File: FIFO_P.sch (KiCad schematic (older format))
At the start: 51 parts, among them J1 Vin +, J2 Vin -, J3 Conn_Coaxial, SW1 Rotary_Encoder_61C, U1 SN74LVC2G157_MUX_TI, U10 AD7840, U2 IDT_ICS551, U3 LTC1740, U4 ARDUINO_DUE_FIFO_P_COMMANDS, U5 IDT_72V2105, U6 TXB0104, U7 TXB0104, U8 TXB0104, U9 TXB0104

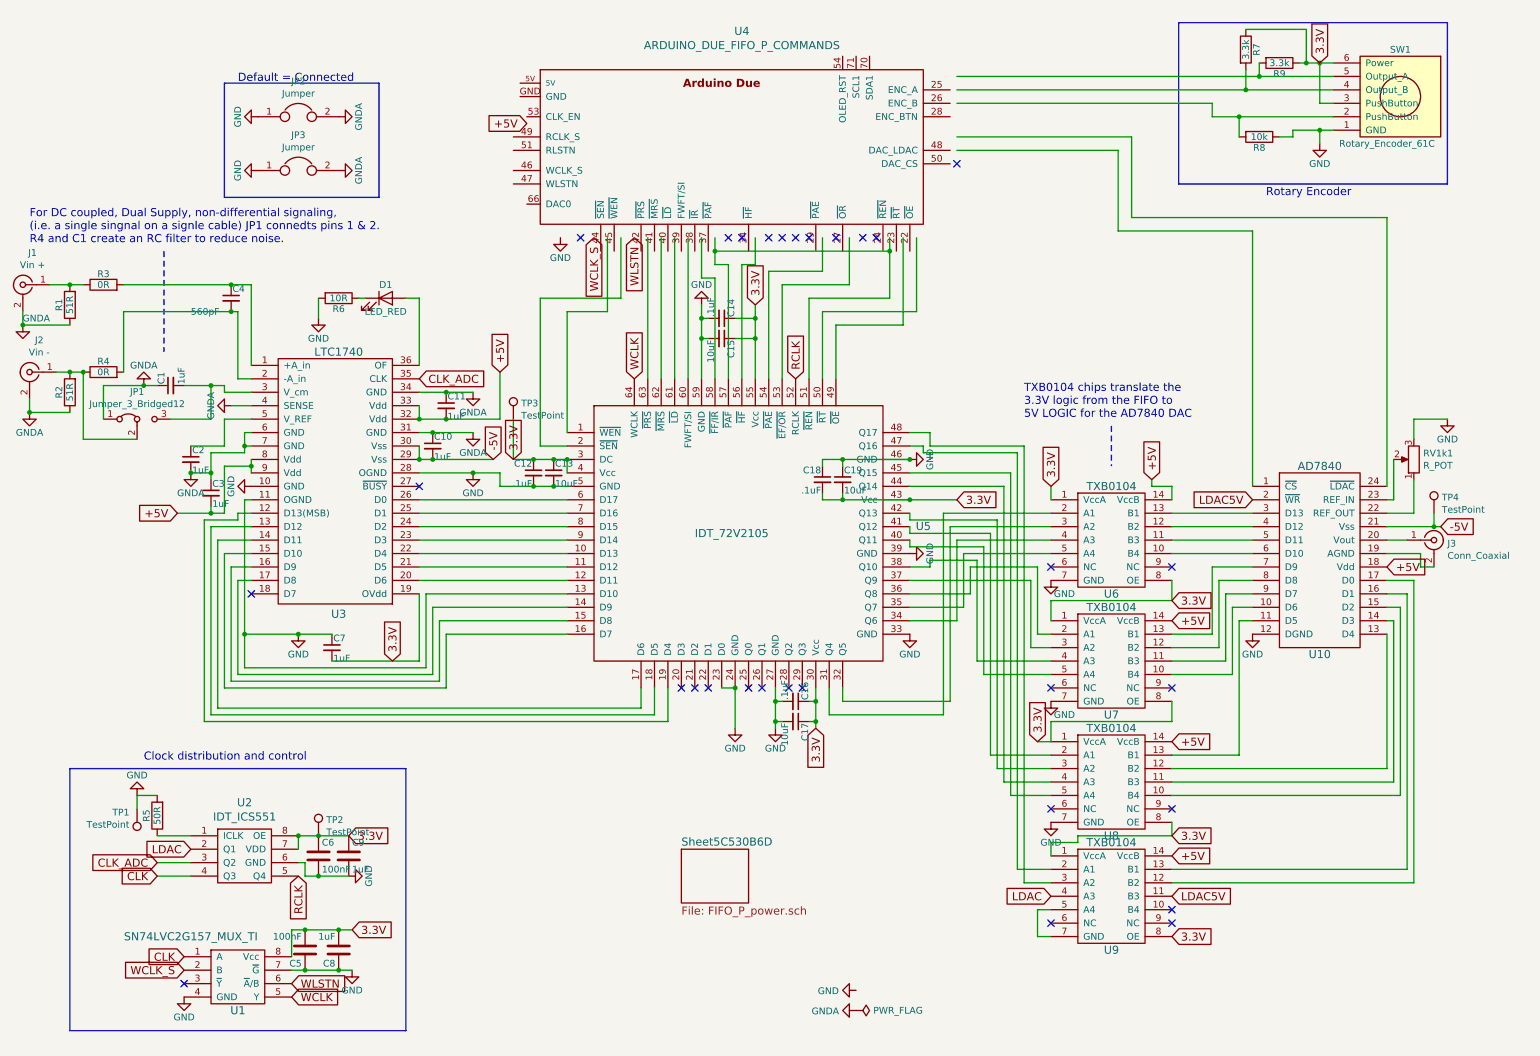
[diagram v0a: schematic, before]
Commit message: Fix arduino header, started laying out connectors
The pins used were changed, so the old code must be rewritten to use the new pins and port D instead of port A.
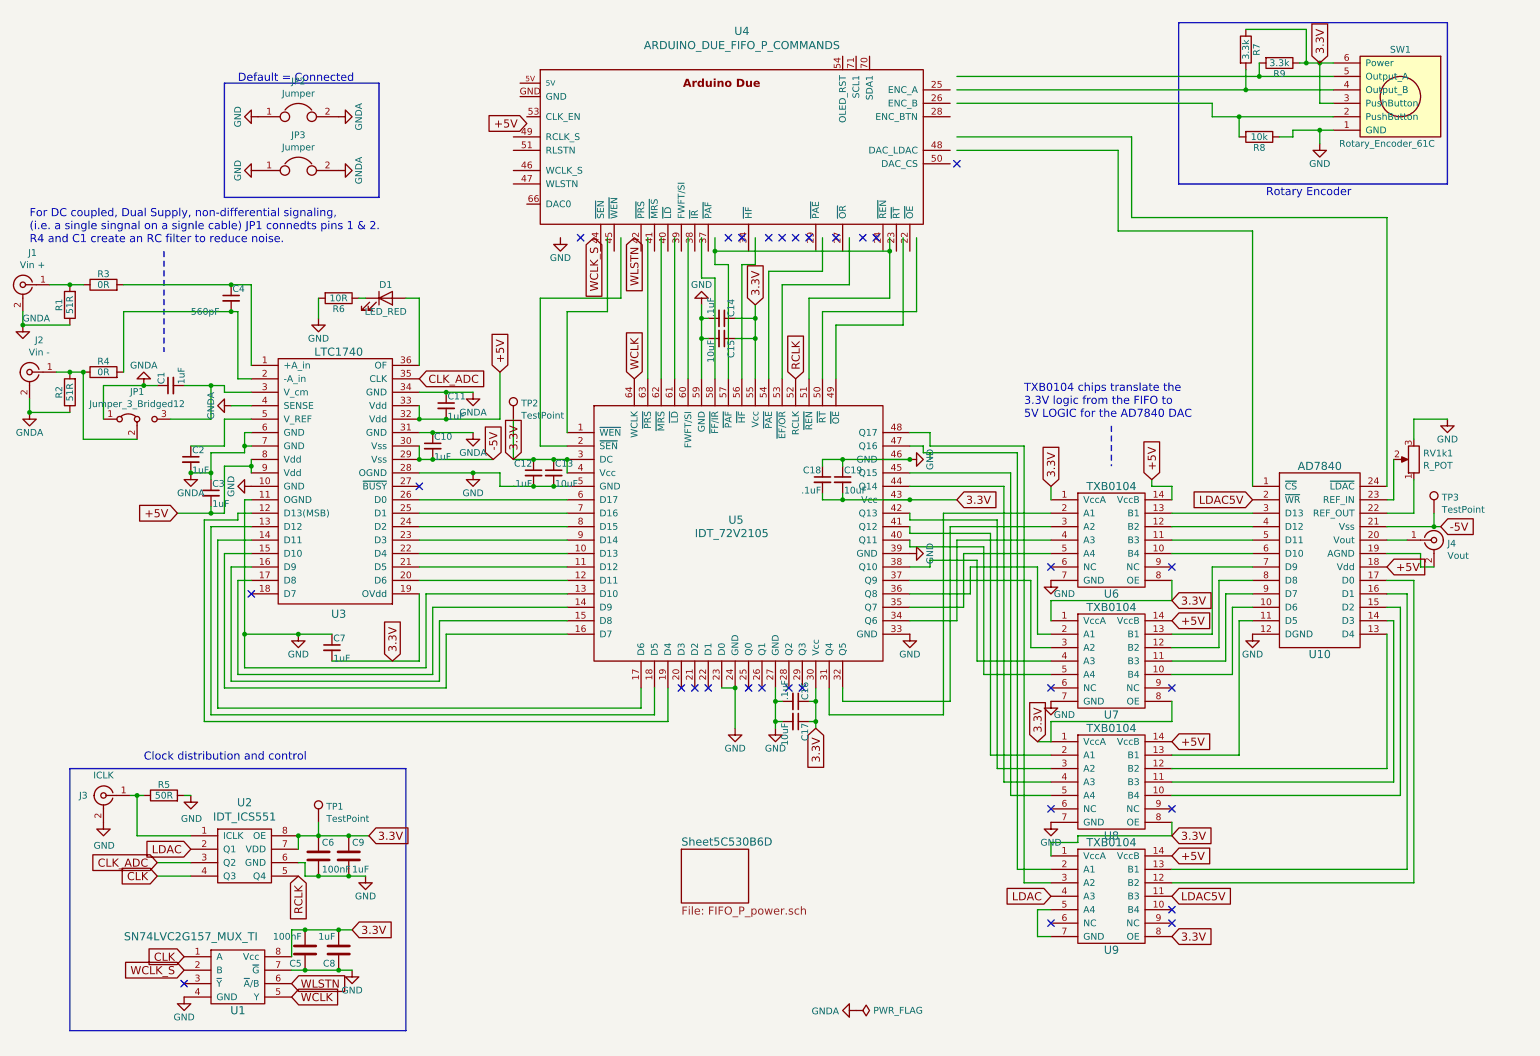
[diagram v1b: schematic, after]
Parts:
- removed TP1: TestPoint, FIFO_P:Test_Pin, symbol Connector:TestPoint
- added J3: ICLK, Connector_Coaxial:BNC_TEConnectivity_1478204_Vertical, symbol Connector:Conn_Coaxial
- J4: renamed from J3; value Conn_Coaxial -> Vout
- renumbered TP2 to TP1, TP3 to TP2, TP4 to TP3
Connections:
- wire segments 358 -> 363
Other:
- moved on the sheet: R5, TP1

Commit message: ADC to FIFO routing
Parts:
- U5: footprint Package_QFP:LQFP-160_24x24mm_P0.5mm -> Package_QFP:LQFP-64_14x14mm_P0.8mm
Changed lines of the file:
@@
 F 0 "U5" H 5650 4200 60  0000 L CNN
 F 1 "IDT_72V2105" H 5400 4100 60  0000 L CNN
-F 2 "Package_QFP:LQFP-160_24x24mm_P0.5mm" H 5700 4100 60  0001 C CNN
+F 2 "Package_QFP:LQFP-64_14x14mm_P0.8mm" H 5700 4100 60  0001 C CNN
 F 3 "" H 5700 4100 60  0000 C CNN
 	1    5700 4100

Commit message: Most routing done
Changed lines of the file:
@@
 	0    1    1    0
 $EndComp
+$Comp
+L power:GND #PWR0101
+U 1 1 5D0F24EC
+P 7950 7100
+F 0 "#PWR0101" H 7950 6850 50  0001 C CNN
+F 1 "GND" H 7955 6927 50  0000 C CNN
+F 2 "" H 7950 7100 50  0001 C CNN
+F 3 "" H 7950 7100 50  0001 C CNN
+	1    7950 7100
+	1    0    0    -1
+$EndComp
+Connection ~ 7950 7100
 $EndSCHEMATC

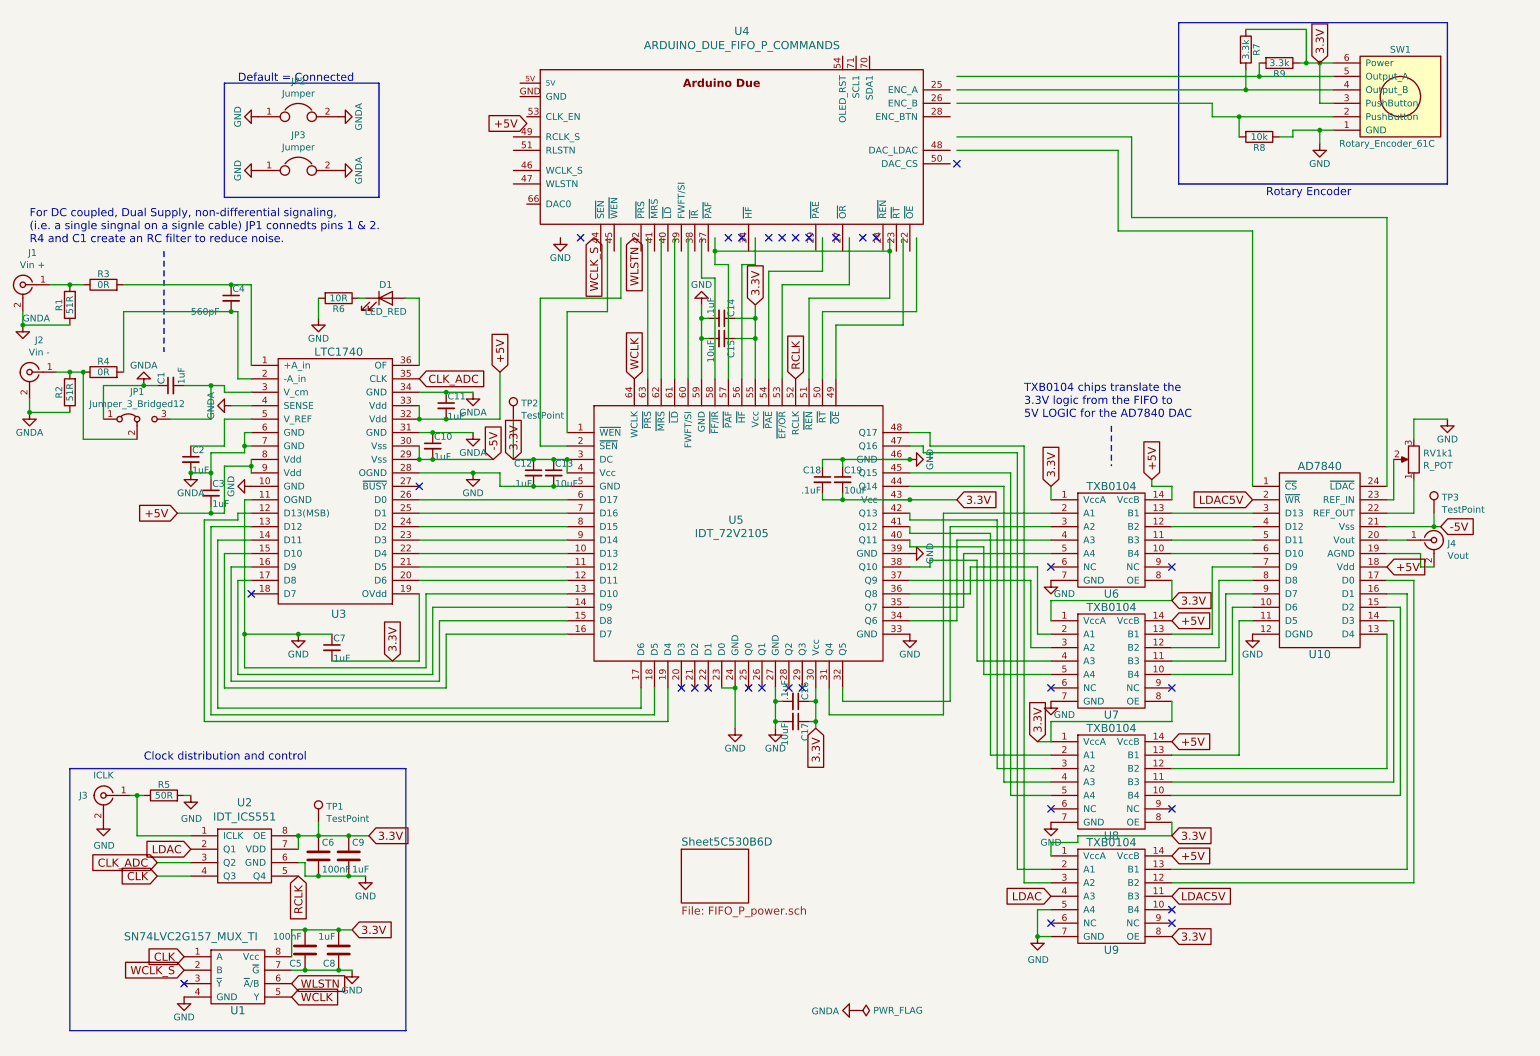
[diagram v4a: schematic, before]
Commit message: Partial jumpers
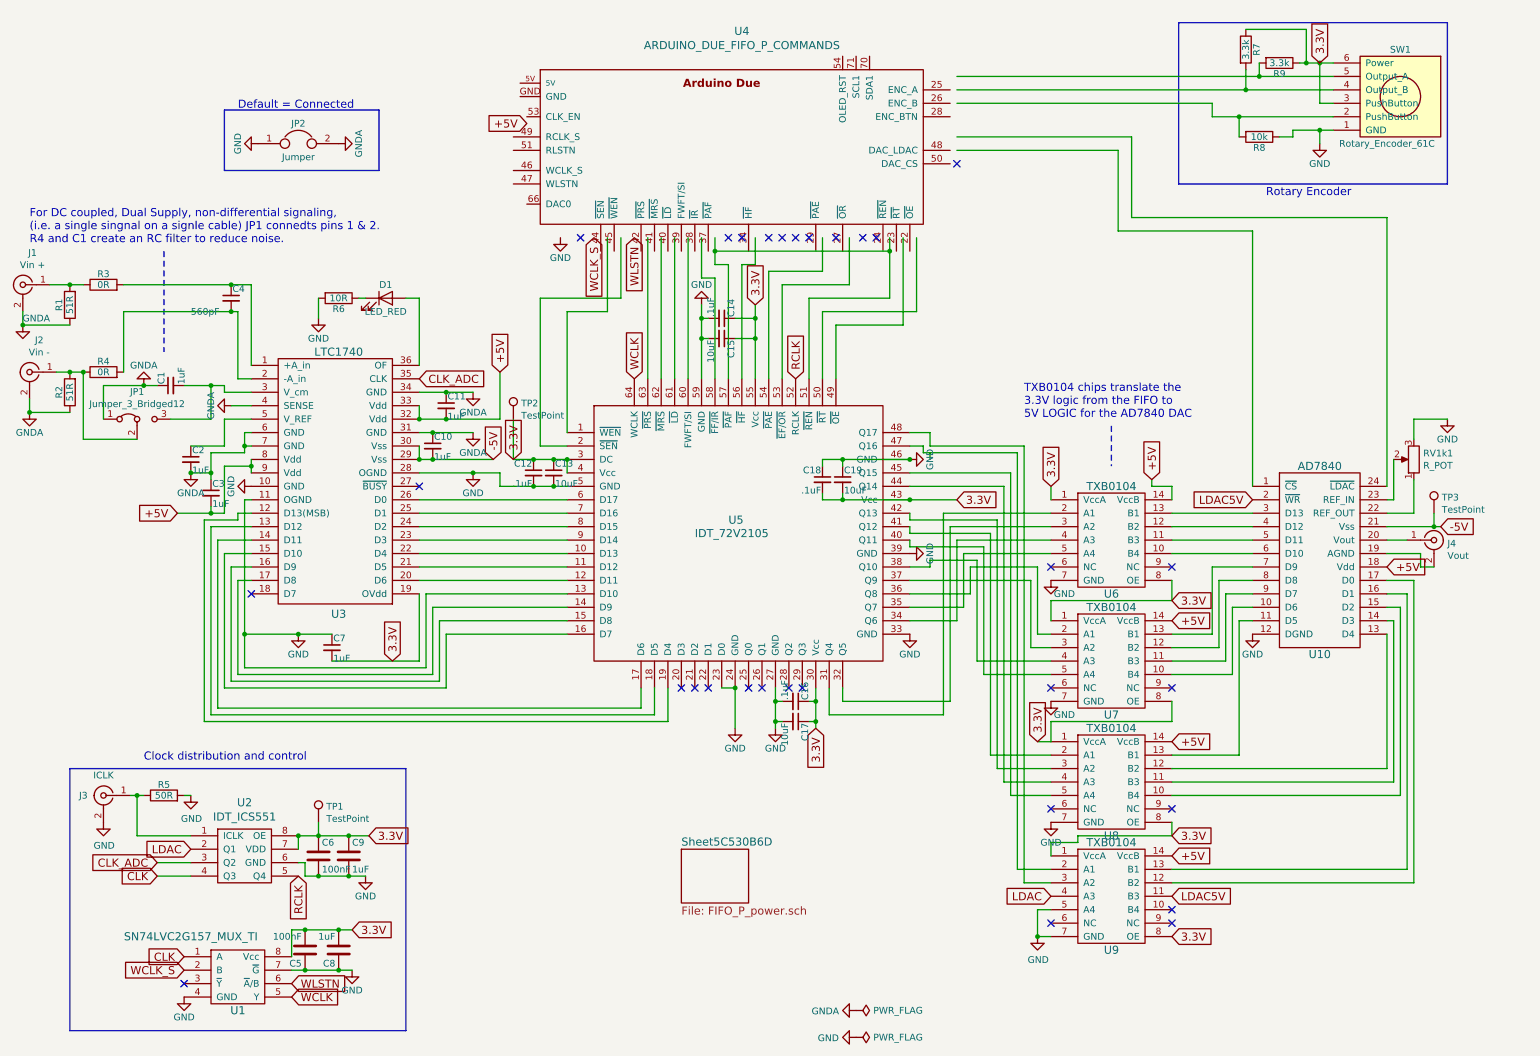
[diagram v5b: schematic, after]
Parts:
- removed JP3: Jumper, Connector_PinHeader_2.54mm:PinHeader_1x02_P2.54mm_Vertical, symbol Device:Jumper
- JP1: footprint Connector_PinHeader_2.54mm:PinHeader_1x02_P2.54mm_Vertical -> Jumper:SolderJumper-3_P1.3mm_Open_RoundedPad1.0x1.5mm
- R3, R4: footprint Resistor_THT:R_Axial_DIN0204_L3.6mm_D1.6mm_P7.62mm_Horizontal -> Resistor_THT:R_Axial_DIN0204_L3.6mm_D1.6mm_P5.08mm_Horizontal
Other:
- moved on the sheet: JP2
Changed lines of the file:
@@
 F 0 "R3" V 1080 2250 50  0000 C CNN
 F 1 "0R" V 1000 2250 50  0000 C CNN
-F 2 "Resistor_THT:R_Axial_DIN0204_L3.6mm_D1.6mm_P7.62mm_Horizontal" V 930 2250 50  0001 C CNN
+F 2 "Resistor_THT:R_Axial_DIN0204_L3.6mm_D1.6mm_P5.08mm_Horizontal" V 930 2250 50  0001 C CNN
 F 3 "" H 1000 2250 50  0000 C CNN
 	1    1000 2250
@@
 F 0 "R4" V 1080 2900 50  0000 C CNN
 F 1 "0R" V 1000 2900 50  0000 C CNN
-F 2 "Resistor_THT:R_Axial_DIN0204_L3.6mm_D1.6mm_P7.62mm_Horizontal" V 930 2900 50  0001 C CNN
+F 2 "Resistor_THT:R_Axial_DIN0204_L3.6mm_D1.6mm_P5.08mm_Horizontal" V 930 2900 50  0001 C CNN
 F 3 "" H 1000 2900 50  0000 C CNN
 	1    1000 2900
@@
 L power:GND #PWR010
 U 1 1 592DEA1F
-P 2150 1000
-F 0 "#PWR010" H 2150 750 50  0001 C CNN
-F 1 "GND" H 2150 850 50  0000 C CNN
-F 2 "" H 2150 1000 50  0000 C CNN
-F 3 "" H 2150 1000 50  0000 C CNN
-	1    2150 1000
+P 2150 1200
+F 0 "#PWR010" H 2150 950 50  0001 C CNN
+F 1 "GND" H 2150 1050 50  0000 C CNN
+F 2 "" H 2150 1200 50  0000 C CNN
+F 3 "" H 2150 1200 50  0000 C CNN
+	1    2150 1200
 	0    1    1    0
 $EndComp
@@
 L power:GNDA #PWR014
 U 1 1 592DEAA9
-P 2750 1000
-F 0 "#PWR014" H 2750 750 50  0001 C CNN
-F 1 "GNDA" H 2750 850 50  0000 C CNN
-F 2 "" H 2750 1000 50  0000 C CNN
-F 3 "" H 2750 1000 50  0000 C CNN
-	1    2750 1000
-	0    -1   -1   0
-$EndComp
-$Comp
-L power:GND #PWR011
-U 1 1 592DEB87
-P 2150 1400
-F 0 "#PWR011" H 2150 1150 50  0001 C CNN
-F 1 "GND" H 2150 1250 50  0000 C CNN
-F 2 "" H 2150 1400 50  0000 C CNN
-F 3 "" H 2150 1400 50  0000 C CNN
-	1    2150 1400
-	0    1    1    0
-$EndComp
-$Comp
-L power:GNDA #PWR015
-U 1 1 592DEB8D
-P 2750 1400
-F 0 "#PWR015" H 2750 1150 50  0001 C CNN
-F 1 "GNDA" H 2750 1250 50  0000 C CNN
-F 2 "" H 2750 1400 50  0000 C CNN
-F 3 "" H 2750 1400 50  0000 C CNN
-	1    2750 1400
+P 2750 1200
+F 0 "#PWR014" H 2750 950 50  0001 C CNN
+F 1 "GNDA" H 2750 1050 50  0000 C CNN
+F 2 "" H 2750 1200 50  0000 C CNN
+F 3 "" H 2750 1200 50  0000 C CNN
+	1    2750 1200
 	0    -1   -1   0
 $EndComp
@@
 	1    0    0    -1
 $EndComp
-Text Notes 2000 750  0    60   ~ 0
+Text Notes 2000 950  0    60   ~ 0
 Default = Connected
 Wire Bus Line
-	1900 750  3050 750
+	1900 950  3050 950
 Wire Bus Line
-	3050 750  3050 1600
+	3050 950  3050 1400
 Wire Bus Line
-	3050 1600 1900 1600
+	3050 1400 1900 1400
 Wire Bus Line
-	1900 1600 1900 750
+	1900 1400 1900 950
 Wire Bus Line
 	750  5850 750  7800
@@
 F 0 "JP1" H 1250 3454 50  0000 C CNN
 F 1 "Jumper_3_Bridged12" H 1250 3363 50  0000 C CNN
-F 2 "Connector_PinHeader_2.54mm:PinHeader_1x02_P2.54mm_Vertical" H 1250 3250 50  0001 C CNN
+F 2 "Jumper:SolderJumper-3_P1.3mm_Open_RoundedPad1.0x1.5mm" H 1250 3250 50  0001 C CNN
 F 3 "~" H 1250 3250 50  0001 C CNN
 	1    1250 3250
@@
 L Device:Jumper JP2
 U 1 1 5D116186
-P 2450 1000
-F 0 "JP2" H 2450 1264 50  0000 C CNN
-F 1 "Jumper" H 2450 1173 50  0000 C CNN
-F 2 "Connector_PinHeader_2.54mm:PinHeader_1x02_P2.54mm_Vertical" H 2450 1000 50  0001 C CNN
-F 3 "~" H 2450 1000 50  0001 C CNN
-	1    2450 1000
-	1    0    0    -1
-$EndComp
-$Comp
-L Device:Jumper JP3
-U 1 1 5D11779A
-P 2450 1400
-F 0 "JP3" H 2450 1664 50  0000 C CNN
-F 1 "Jumper" H 2450 1573 50  0000 C CNN
-F 2 "Connector_PinHeader_2.54mm:PinHeader_1x02_P2.54mm_Vertical" H 2450 1400 50  0001 C CNN
-F 3 "~" H 2450 1400 50  0001 C CNN
-	1    2450 1400
+P 2450 1200
+F 0 "JP2" H 2450 1350 50  0000 C CNN
+F 1 "Jumper" H 2450 1100 50  0000 C CNN
+F 2 "Connector_PinHeader_2.54mm:PinHeader_1x02_P2.54mm_Vertical" H 2450 1200 50  0001 C CNN
+F 3 "~" H 2450 1200 50  0001 C CNN
+	1    2450 1200
 	1    0    0    -1
 $EndComp
@@
 $EndComp
 Connection ~ 7950 7100
+$Comp
+L power:GND #PWR043
+U 1 1 5D14AE87
+P 6600 7850
+F 0 "#PWR043" H 6600 7600 50  0001 C CNN
+F 1 "GND" V 6605 7722 50  0000 R CNN
+F 2 "" H 6600 7850 50  0001 C CNN
+F 3 "" H 6600 7850 50  0001 C CNN
+	1    6600 7850
+	0    1    1    0
+$EndComp
+$Comp
+L power:PWR_FLAG #FLG03
+U 1 1 5D14B233
+P 6600 7850
+F 0 "#FLG03" H 6600 7925 50  0001 C CNN
+F 1 "PWR_FLAG" V 6600 7978 50  0000 L CNN
+F 2 "" H 6600 7850 50  0001 C CNN
+F 3 "~" H 6600 7850 50  0001 C CNN
+	1    6600 7850
+	0    1    1    0
+$EndComp
 $EndSCHEMATC

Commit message: Moved power
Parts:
- U5: footprint Package_QFP:LQFP-64_14x14mm_P0.8mm -> FIFO_P:LQFP-64_14x14mm_P0.8mm_HandSolder
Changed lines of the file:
@@
 F 0 "U5" H 5650 4200 60  0000 L CNN
 F 1 "IDT_72V2105" H 5400 4100 60  0000 L CNN
-F 2 "Package_QFP:LQFP-64_14x14mm_P0.8mm" H 5700 4100 60  0001 C CNN
+F 2 "FIFO_P:LQFP-64_14x14mm_P0.8mm_HandSolder" H 5700 4100 60  0001 C CNN
 F 3 "" H 5700 4100 60  0000 C CNN
 	1    5700 4100
